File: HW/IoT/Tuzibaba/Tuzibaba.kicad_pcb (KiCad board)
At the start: 2 copper layers, 19 parts, among them J1 1x1 2.54mm male, J11 1x2 2.54mm male, J2 1x5 2.54mm male, J3 1x1 2.54mm male, Q1 IRF4905, Q2 BC338, U1 TL071

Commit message: Add changes made to schem and pcb
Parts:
- removed C1, C2: 100n, For_Rasterboard:C_Disc_D3.0mm_W1.6mm_Pinf
- removed J11: 1x2 2.54mm male, Extra_Common:MOLEX-22-23-2021
- removed J3: 1x1 2.54mm male, Connector_PinHeader_2.54mm:PinHeader_1x01_P2.54mm_Vertical
- removed Q1: IRF4905, Package_TO_SOT_THT:TO-220-3_Vertical
- removed Q2: BC338, For_Rasterboard:TO-92_Inline_inf
- removed R5: 220k, For_Rasterboard:R_Axial_DIN0207_L6.3mm_D2.5mm_P7.62mm_Horizontal
- removed R6: 220k, For_Rasterboard:R_Axial_DIN0207_L6.3mm_D2.5mm_Pinf_Horizontal
- removed R7: 1k5, For_Rasterboard:R_Axial_DIN0207_L6.3mm_D2.5mm_P5.08mm_Vertical
- removed RV1: 250, Potentiometer_THT:Potentiometer_Piher_PT-10-V10_Vertical
- removed RV2: 100k, Potentiometer_THT:Potentiometer_Piher_PT-10-H01_Horizontal
- removed U1: TL071, Package_DIP:DIP-8_W7.62mm
- J1: value 1x1 2.54mm male -> 2x9 2.54mm 90deg female; footprint Connector_PinHeader_2.54mm:PinHeader_1x01_P2.54mm_Vertical -> Connector_PinSocket_2.54mm:PinSocket_2x09_P2.54mm_Vertical
- R1: value 220 -> 10K; footprint For_Rasterboard:R_Axial_DIN0207_L6.3mm_D2.5mm_Pinf_Horizontal -> For_Rasterboard:R_Axial_DIN0207_L6.3mm_D2.5mm_P7.62mm_Horizontal
- R2: value 0.1 -> 10K; footprint Resistor_THT:R_Axial_DIN0207_L6.3mm_D2.5mm_P10.16mm_Horizontal -> For_Rasterboard:R_Axial_DIN0207_L6.3mm_D2.5mm_P7.62mm_Horizontal
- R3: value 220k -> 4.7K; footprint For_Rasterboard:R_Axial_DIN0207_L6.3mm_D2.5mm_Pinf_Horizontal -> For_Rasterboard:R_Axial_DIN0207_L6.3mm_D2.5mm_P7.62mm_Horizontal
- R4: value 220k -> 4.7K
- moved J1 69.3 mm to (109.2, 152.4)
- moved R2 31.5 mm to (173.6, 114.5)
- moved J2 27.2 mm to (169.7, 106.7)
- moved A1 24.7 mm to (132.1, 106.7)
- moved R3 22.7 mm to (173.6, 106.4)
- moved R4 20.2 mm to (173.6, 110.4)
- moved R1 18.7 mm to (173.6, 118.5)
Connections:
- A1 pad 10: unconnected-(A1-Pad10) -> /D1
- A1 pad 13: unconnected-(A1-Pad13) -> Net-(A1-Pad13)
- A1 pad 14: unconnected-(A1-Pad14) -> Net-(A1-Pad14)
- A1 pad 22: unconnected-(A1-Pad22) -> /D7
- A1 pad 26: unconnected-(A1-Pad26) -> Net-(A1-Pad26)
- A1 pad 29: unconnected-(A1-Pad29) -> GND
- A1 pad 31: unconnected-(A1-Pad31) -> /SIOD
- A1 pad 32: unconnected-(A1-Pad32) -> /SIOC
- A1 pad 4: unconnected-(A1-Pad4) -> +3V3
- A1 pad 9: /OUT0 -> /D0
- J1 pad 1: Net-(J1-Pad1) -> GND
- J2 pad 3: /ch0/PWM -> unconnected-(J2-Pad3)
- J2 pad 4: /ch0/N -> /N
- R1 pad 1: +5V -> Net-(R1-Pad1)
- R1 pad 2: Net-(R1-Pad2) -> Net-(A1-Pad13)
- R2 pad 1: /ch0/N -> Net-(R1-Pad1)
- R2 pad 2: /ch0/P -> Net-(A1-Pad14)
- R3 pad 1: GNDA -> Net-(R3-Pad1)
- R3 pad 2: /ch0/sub/op/IN+ -> Net-(A1-Pad26)
- R4 pad 1: /ch0/N -> Net-(R3-Pad1)
- R4 pad 2: /ch0/sub/op/IN+ -> unconnected-(R4-Pad2)
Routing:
- net /SIOD: track 0.00 -> 149.9 mm, vias 0 -> 2
- net GND: track 0.00 -> 101.6 mm, vias 0 -> 4
- net /D1: track 0.00 -> 88.9 mm, vias 0 -> 2
- net /SIOC: track 0.00 -> 83.8 mm, vias 0 -> 2
- net /D0: track 0.00 -> 76.2 mm, vias 0 -> 2
- net +3V3: track 0.00 -> 68.6 mm, vias 0 -> 2
- net /D7: track 0.00 -> 61.0 mm, vias 0 -> 2

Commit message: Update schematic and pcb
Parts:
- moved J2 7.63 mm to (171.4, 114.1)
- moved R1 7.63 mm to (175.3, 126.0)
- moved R2 7.63 mm to (175.3, 121.9)
- moved R3 7.63 mm to (175.3, 113.8)
- moved R4 7.63 mm to (175.3, 117.9)
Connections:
- net Net-(A1-Pad26) renamed /S_XCLK
- A1 pad 11: unconnected-(A1-Pad11) -> /D2
- A1 pad 12: unconnected-(A1-Pad12) -> /D3
- A1 pad 13: Net-(A1-Pad13) -> unconnected-(A1-Pad13)
- A1 pad 14: Net-(A1-Pad14) -> unconnected-(A1-Pad14)
- A1 pad 17: /DIS0 -> /PCLK
- A1 pad 18: unconnected-(A1-Pad18) -> /VSYN0
- A1 pad 19: unconnected-(A1-Pad19) -> /D4
- A1 pad 20: unconnected-(A1-Pad20) -> /D5
- A1 pad 23: unconnected-(A1-Pad23) -> /HREF
- J1 pad 11: unconnected-(J1-Pad11) -> /D4
- J1 pad 12: unconnected-(J1-Pad12) -> /D5
- J1 pad 13: unconnected-(J1-Pad13) -> /D2
- J1 pad 14: unconnected-(J1-Pad14) -> /D3
- J1 pad 17: unconnected-(J1-Pad17) -> GND
- J1 pad 18: unconnected-(J1-Pad18) -> +3V3
- J1 pad 5: unconnected-(J1-Pad5) -> /HREF
- J1 pad 6: unconnected-(J1-Pad6) -> /VSYN0
- J1 pad 7: unconnected-(J1-Pad7) -> /XCLK
- J1 pad 8: unconnected-(J1-Pad8) -> /PCLK
- R1 pad 1: Net-(R1-Pad1) -> /SIOD
- R1 pad 2: Net-(A1-Pad13) -> +3V3
- R2 pad 1: Net-(R1-Pad1) -> +3V3
- R2 pad 2: Net-(A1-Pad14) -> /SIOC
- R3 pad 1: Net-(R3-Pad1) -> /XCLK
- R4 pad 1: Net-(R3-Pad1) -> /XCLK
- R4 pad 2: unconnected-(R4-Pad2) -> GND
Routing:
- net /D5: track 0.00 -> 58.7 mm, vias 0 -> 2
- net /PCLK: track 0.00 -> 45.7 mm, vias 0 -> 2
- net /VSYN0: track 0.00 -> 45.7 mm, vias 0 -> 2

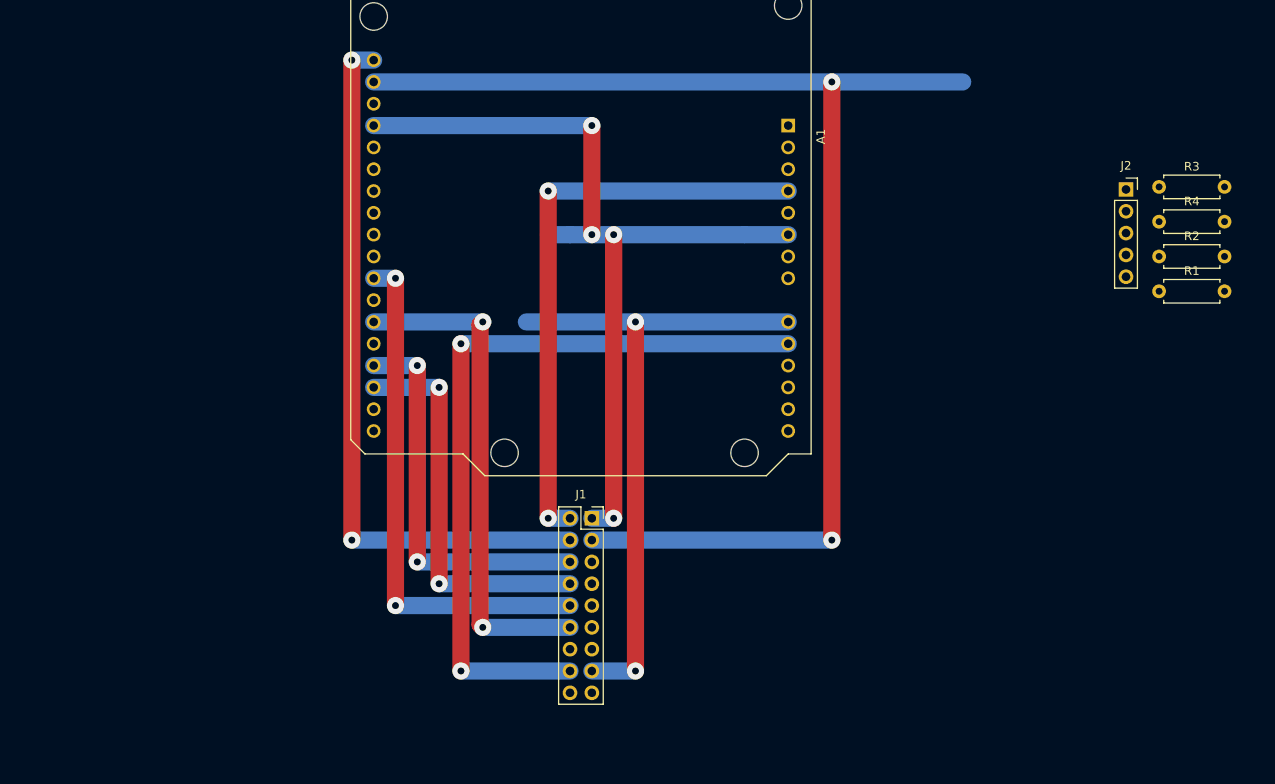
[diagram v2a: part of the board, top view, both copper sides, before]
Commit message: Update schematic and pcb for camera
FOR IT IS FINALLY WORKING
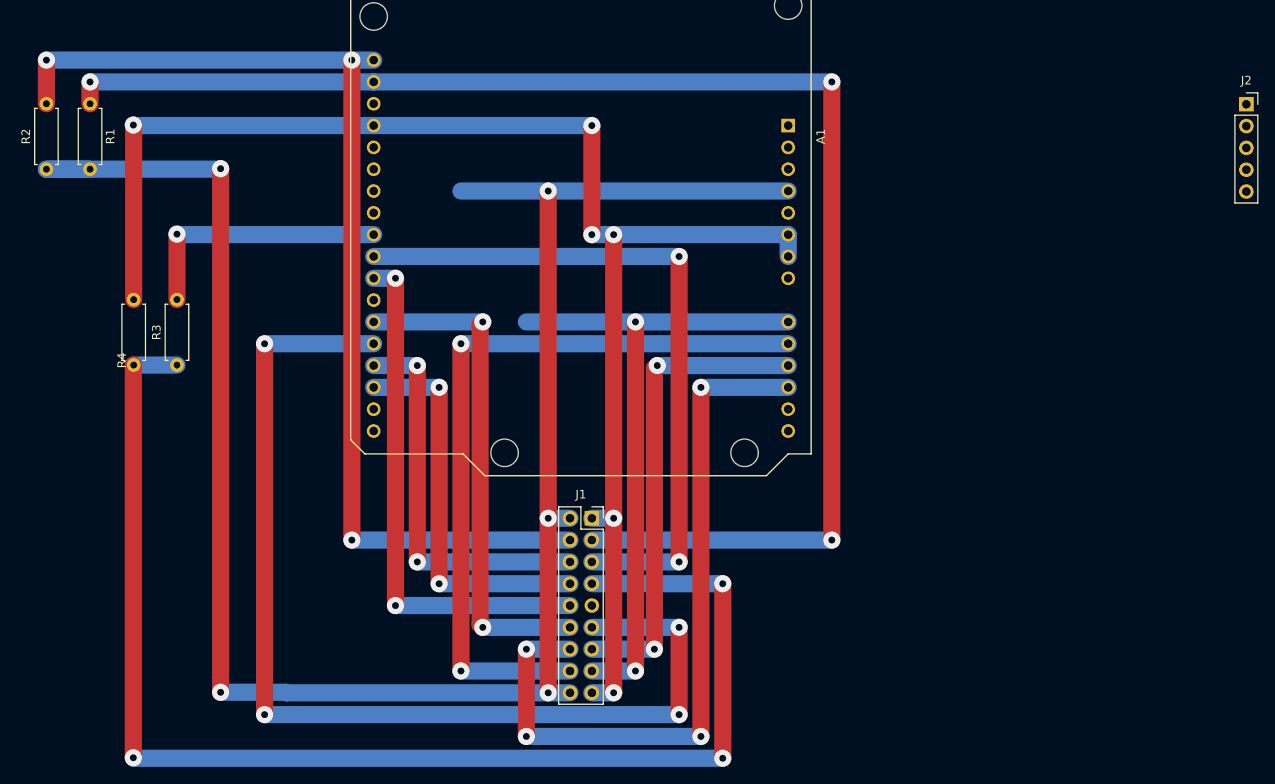
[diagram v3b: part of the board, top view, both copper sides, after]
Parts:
- moved R2 129.9 mm to (45.7, 111.8), turned to 90 degrees
- moved R1 126.4 mm to (50.8, 104.1), turned to -90 degrees
- moved R4 120.5 mm to (55.9, 134.6), turned to 90 degrees
- moved R3 116.2 mm to (60.9, 134.6), turned to 90 degrees
- moved J2 17.2 mm to (185.4, 104.2)
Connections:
- A1 pad 21: unconnected-(A1-Pad21) -> /D6
- A1 pad 24: unconnected-(A1-Pad24) -> /S_XCLK
- A1 pad 26: /S_XCLK -> unconnected-(A1-Pad26)
- J2 pad 5: GND -> unconnected-(J2-Pad5)
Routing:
- net +3V3: track 68.6 -> 226.1 mm, vias 2 -> 5
- net /XCLK: track 0.00 -> 155.0 mm, vias 0 -> 3
- net /D4: track 0.00 -> 124.5 mm, vias 0 -> 4
- net /D3: track 0.00 -> 86.4 mm, vias 0 -> 4
- net /HREF: track 0.00 -> 81.3 mm, vias 0 -> 2
- net GND: track 101.6 -> 170.3 mm, vias 4 -> 6
- net /D2: track 0.00 -> 55.7 mm, vias 0 -> 2
- net /SIOC: track 83.8 -> 124.5 mm, vias 2 -> 3
- net /S_XCLK: track 0.00 -> 30.5 mm, vias 0 -> 1
- net /SIOD: track 149.9 -> 170.2 mm, vias 2 -> 3

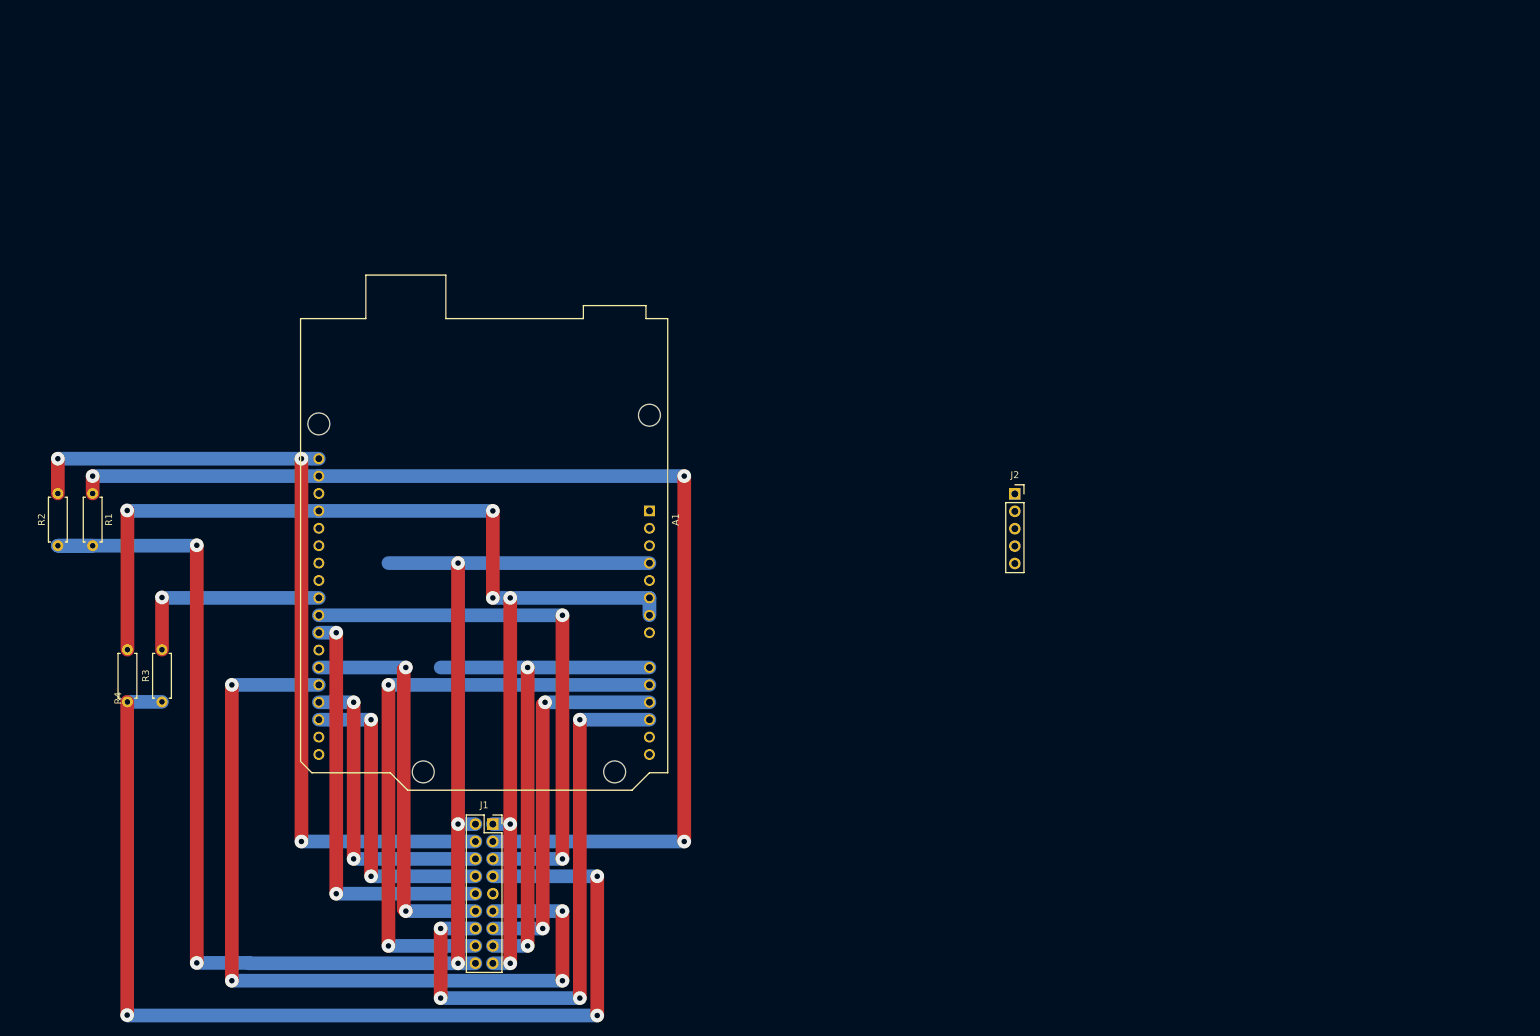
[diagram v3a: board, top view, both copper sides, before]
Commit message: Finalize schematic and pcb for arduino with camera
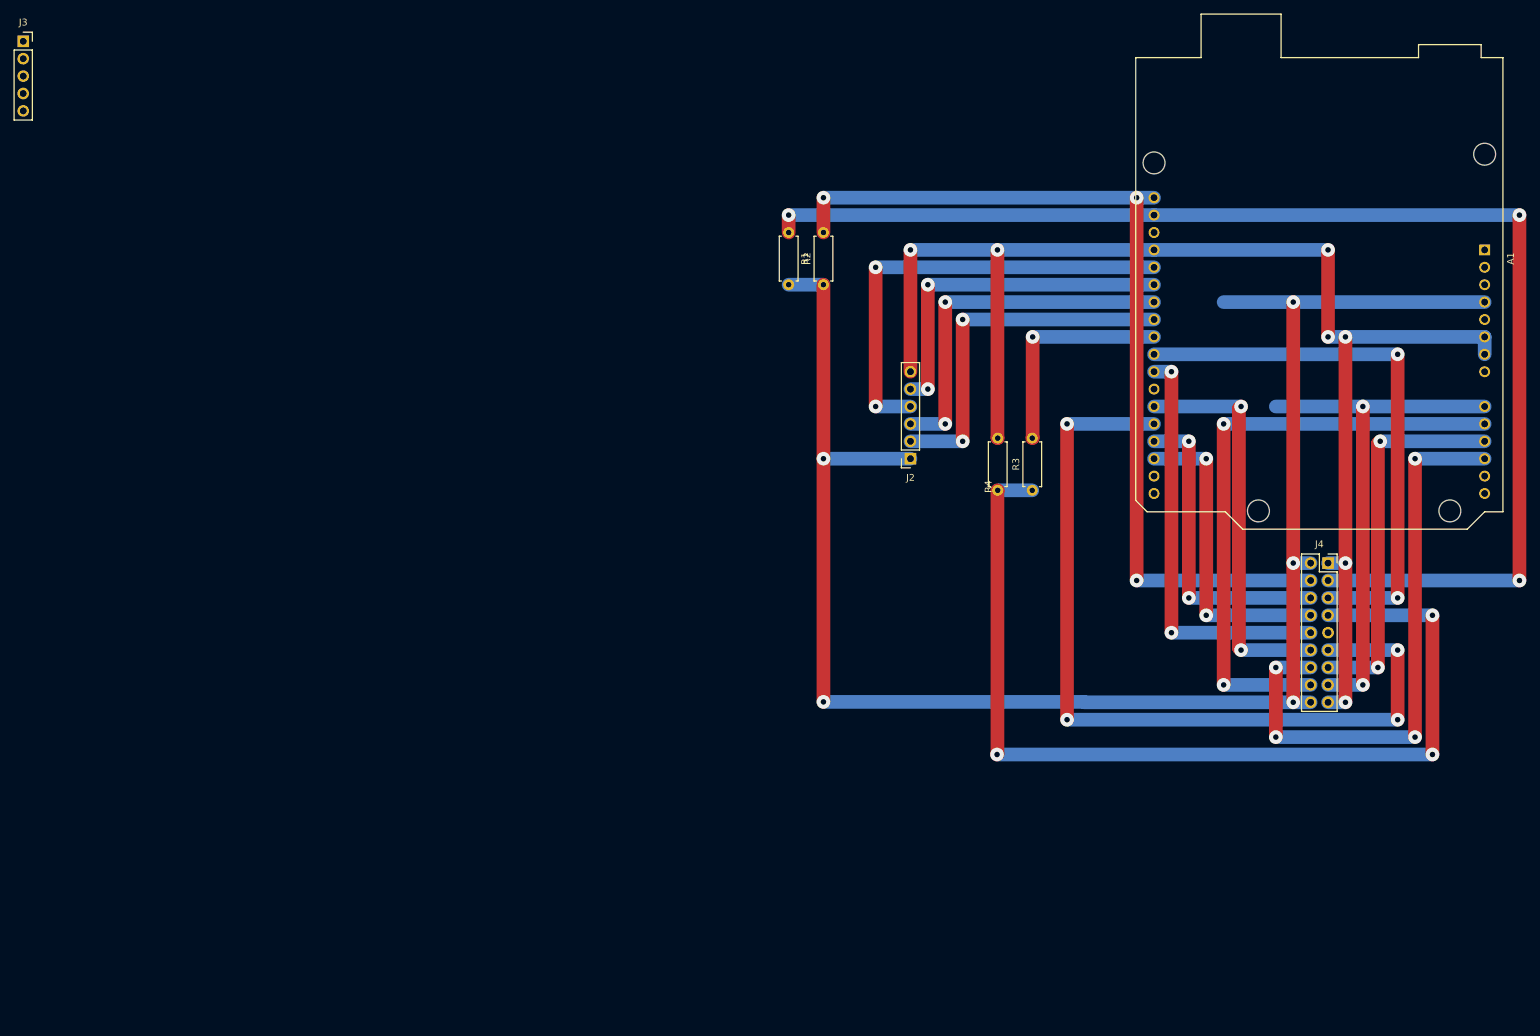
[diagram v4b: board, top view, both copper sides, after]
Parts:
- added J2: 1x6 2.54mm male, Connector_PinSocket_2.54mm:PinSocket_1x06_P2.54mm_Vertical, F.Cu at (170.2, 99.1)
- moved J3 159.1 mm to (40.7, 38.1)
- moved R3 130.7 mm to (188.0, 103.7)
- moved R4 130.7 mm to (182.9, 103.7)
- moved A1 127.7 mm to (254.0, 68.6)
- moved J4 127.7 mm to (231.1, 114.3)
- moved R2 118.1 mm to (157.5, 73.7)
- moved R1 108.5 mm to (152.4, 66.0)
- renumbered J2 to J3, J1 to J4
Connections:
- A1 pad 25: unconnected-(A1-Pad25) -> /CS
- A1 pad 26: unconnected-(A1-Pad26) -> /MOSI
- A1 pad 27: unconnected-(A1-Pad27) -> /MISO
- A1 pad 28: unconnected-(A1-Pad28) -> /CLK
- J3 pad 4: /N -> unconnected-(J3-Pad4)
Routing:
- net /CLK: track 0.00 -> 66.0 mm, vias 0 -> 2
- net /MOSI: track 0.00 -> 53.3 mm, vias 0 -> 2
- net /CS: track 0.00 -> 53.3 mm, vias 0 -> 2
- net /MISO: track 0.00 -> 50.8 mm, vias 0 -> 2
- net GND: track 170.3 -> 202.8 mm, vias 6 -> 7
- net +3V3: track 226.1 -> 248.9 mm
- net /SIOD: track 170.2 -> 190.5 mm
- net /XCLK: track 155.0 -> 142.8 mm
- net /SIOC: track 124.5 -> 134.6 mm
- net /S_XCLK: track 30.5 -> 32.5 mm

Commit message: Add 3pin connector for UART w/ 2nd arduino
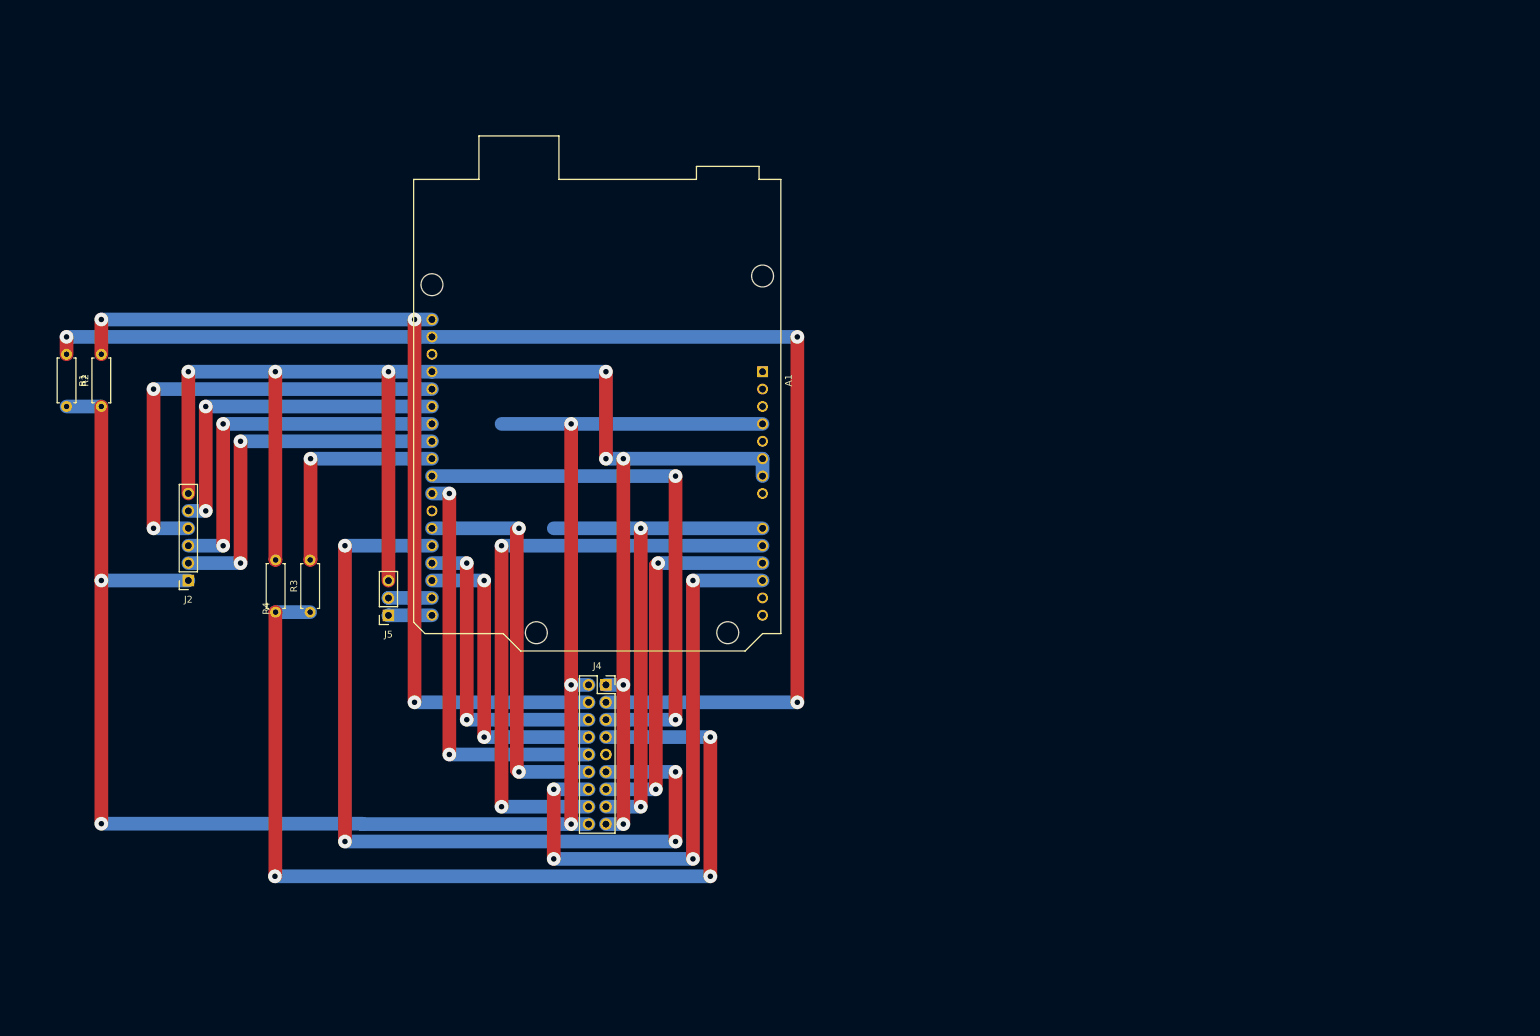
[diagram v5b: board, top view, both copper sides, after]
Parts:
- removed J3: 1x5 2.54mm male, Connector_PinSocket_2.54mm:PinSocket_1x05_P2.54mm_Vertical
- added J5: 1x3 2.54mm male, Connector_PinSocket_2.54mm:PinSocket_1x03_P2.54mm_Vertical, F.Cu at (94.0, 121.9)
- moved J2 106.9 mm to (64.8, 116.8)
- moved R3 106.9 mm to (82.5, 121.5)
- moved A1 106.9 mm to (148.6, 86.4)
- moved R1 106.9 mm to (47.0, 83.8)
- moved R2 106.9 mm to (52.1, 91.4)
- moved J4 106.9 mm to (125.7, 132.1)
- moved R4 106.9 mm to (77.5, 121.5)
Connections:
- A1 pad 15: unconnected-(A1-Pad15) -> /RX
- A1 pad 16: unconnected-(A1-Pad16) -> /TX
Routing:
- net GND: track 202.8 -> 233.3 mm, vias 7 -> 8
- net /TX: track 0.00 -> 6.36 mm
- net /RX: track 0.00 -> 6.36 mm
